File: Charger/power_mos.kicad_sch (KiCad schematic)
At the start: 7 parts, among them Q1 MMBT3906, Q2 AO3400A

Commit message: charger WIP
Most footprints assigned, shunt drawn in schem
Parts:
- renumbered D7 to D9
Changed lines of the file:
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@@
 		(in_pos_files yes)
 		(dnp no)
-		(property "Reference" "D7"
+		(property "Reference" "D9"
 			(at 126.365 86.233 90)
 			(show_name no)
@@
 			(project "Charger"
 				(path "/ba218c5d-b6ee-4635-9cf5-de406e83bbdf/5e21c6b0-7567-43d6-bd0d-213ea70bf189"
-					(reference "D7")
+					(reference "D9")
 					(unit 1)
 				)
 				(path "/ba218c5d-b6ee-4635-9cf5-de406e83bbdf/d20a1503-06d5-45b3-92f8-a558cbee8499"
-					(reference "D8")
+					(reference "D10")
 					(unit 1)
 				)

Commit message: edited VCU and  charger
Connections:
- net VIN: no longer Q1.2 (E)
- new net +5V: Q1.2 (E)
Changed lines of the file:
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@@
-	)
-	(junction
-		(at 130.81 68.58)
-		(diameter 0)
-		(color 0 0 0 0)
 	)
 	(junction
@@
 	(wire
 		(pts
-			(xy 128.27 68.58) (xy 130.81 68.58)
-		)
-		(stroke
-			(width 0)
-			(type default)
-		)
-	)
-	(wire
-		(pts
 			(xy 148.59 72.39) (xy 153.67 72.39)
 		)
@@
 		)
 	)
-	(wire
-		(pts
-			(xy 139.7 68.58) (xy 130.81 68.58)
-		)
-		(stroke
-			(width 0)
-			(type default)
+	(hierarchical_label "VIN"
+		(shape input)
+		(at 139.7 68.58 180)
+		(effects
+			(font
+				(size 1.27 1.27)
+			)
+			(justify right)
 		)
 	)
@@
 			)
 			(justify left)
-		)
-	)
-	(hierarchical_label "VIN"
-		(shape input)
-		(at 128.27 68.58 180)
-		(effects
-			(font
-				(size 1.27 1.27)
-			)
-			(justify right)
 		)
 	)
@@
 					(unit 1)
 				)
+			)
+		)
+	)
+	(symbol
+		(lib_id "power:+5V")
+		(at 130.81 68.58 0)
+		(unit 1)
+		(body_style 1)
+		(exclude_from_sim no)
+		(in_bom yes)
+		(on_board yes)
+		(in_pos_files yes)
+		(dnp no)
+		(fields_autoplaced yes)
+		(property "Reference" "#PWR0103"
+			(at 130.81 72.39 0)
+			(hide yes)
+			(show_name no)
+			(do_not_autoplace no)
+			(effects
+				(font
+					(size 1.27 1.27)
+				)
+			)
+		)
+		(property "Value" "+5V"
+			(at 130.81 63.5 0)
+			(show_name no)
+			(do_not_autoplace no)
+			(effects
+				(font
+					(size 1.27 1.27)
+				)
+			)
+		)
+		(property "Footprint" ""
+			(at 130.81 68.58 0)
+			(hide yes)
+			(show_name no)
+			(do_not_autoplace no)
+			(effects
+				(font
+					(size 1.27 1.27)
+				)
+			)
+		)
+		(property "Datasheet" ""
+			(at 130.81 68.58 0)
+			(hide yes)
+			(show_name no)
+			(do_not_autoplace no)
+			(effects
+				(font
+					(size 1.27 1.27)
+				)
+			)
+		)
+		(property "Description" "Power symbol creates a global label with name \"+5V\""
+			(at 130.81 68.58 0)
+			(hide yes)
+			(show_name no)
+			(do_not_autoplace no)
+			(effects
+				(font
+					(size 1.27 1.27)
+				)
+			)
+		)
+		(pin "1"
+		)
+		(instances
+			(project "Charger"
+				(path "/ba218c5d-b6ee-4635-9cf5-de406e83bbdf/5e21c6b0-7567-43d6-bd0d-213ea70bf189"
+					(reference "#PWR0103")
+					(unit 1)
+				)
+				(path "/ba218c5d-b6ee-4635-9cf5-de406e83bbdf/d20a1503-06d5-45b3-92f8-a558cbee8499"
+					(reference "#PWR0104")
+					(unit 1)
+				)

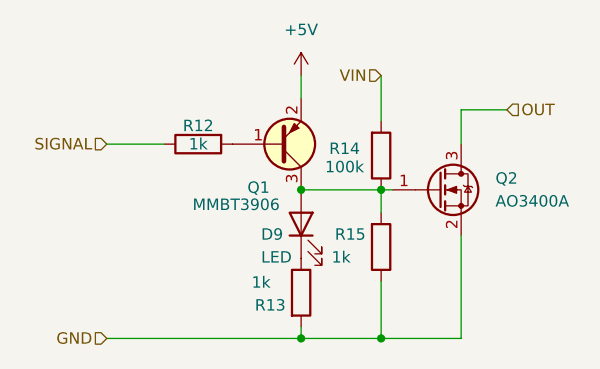
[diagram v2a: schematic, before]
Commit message: Charger 0.1.0 PCB ready for review
Silkscreen adjustments have not been finished yet
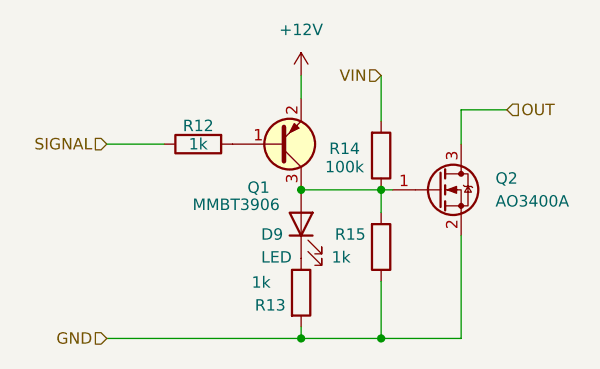
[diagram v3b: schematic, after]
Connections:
- net +5V renamed +12V
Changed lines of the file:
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@@
 	(generator_version "10.0")
 	(paper "A4")
+	(title_block
+		(date "2026-08-20")
+		(rev "0.1.1")
+	)
 	(junction
 		(at 130.81 81.28)
@@
 				(path "/ba218c5d-b6ee-4635-9cf5-de406e83bbdf/d20a1503-06d5-45b3-92f8-a558cbee8499"
 					(reference "R17")
-					(unit 1)
-				)
-			)
-		)
-	)
-	(symbol
-		(lib_id "power:+5V")
-		(at 130.81 68.58 0)
-		(unit 1)
-		(body_style 1)
-		(exclude_from_sim no)
-		(in_bom yes)
-		(on_board yes)
-		(in_pos_files yes)
-		(dnp no)
-		(fields_autoplaced yes)
-		(property "Reference" "#PWR0103"
-			(at 130.81 72.39 0)
-			(hide yes)
-			(show_name no)
-			(do_not_autoplace no)
-			(effects
-				(font
-					(size 1.27 1.27)
-				)
-			)
-		)
-		(property "Value" "+5V"
-			(at 130.81 63.5 0)
-			(show_name no)
-			(do_not_autoplace no)
-			(effects
-				(font
-					(size 1.27 1.27)
-				)
-			)
-		)
-		(property "Footprint" ""
-			(at 130.81 68.58 0)
-			(hide yes)
-			(show_name no)
-			(do_not_autoplace no)
-			(effects
-				(font
-					(size 1.27 1.27)
-				)
-			)
-		)
-		(property "Datasheet" ""
-			(at 130.81 68.58 0)
-			(hide yes)
-			(show_name no)
-			(do_not_autoplace no)
-			(effects
-				(font
-					(size 1.27 1.27)
-				)
-			)
-		)
-		(property "Description" "Power symbol creates a global label with name \"+5V\""
-			(at 130.81 68.58 0)
-			(hide yes)
-			(show_name no)
-			(do_not_autoplace no)
-			(effects
-				(font
-					(size 1.27 1.27)
-				)
-			)
-		)
-		(pin "1"
-		)
-		(instances
-			(project "Charger"
-				(path "/ba218c5d-b6ee-4635-9cf5-de406e83bbdf/5e21c6b0-7567-43d6-bd0d-213ea70bf189"
-					(reference "#PWR0103")
-					(unit 1)
-				)
-				(path "/ba218c5d-b6ee-4635-9cf5-de406e83bbdf/d20a1503-06d5-45b3-92f8-a558cbee8499"
-					(reference "#PWR0104")
 					(unit 1)
 				)
@@
 					(unit 1)
 				)
+			)
+		)
+	)
+	(symbol
+		(lib_id "power:+12V")
+		(at 130.81 68.58 0)
+		(unit 1)
+		(body_style 1)
+		(exclude_from_sim no)
+		(in_bom yes)
+		(on_board yes)
+		(in_pos_files yes)
+		(dnp no)
+		(fields_autoplaced yes)
+		(property "Reference" "#PWR010"
+			(at 130.81 72.39 0)
+			(hide yes)
+			(show_name no)
+			(do_not_autoplace no)
+			(effects
+				(font
+					(size 1.27 1.27)
+				)
+			)
+		)
+		(property "Value" "+12V"
+			(at 130.81 63.5 0)
+			(show_name no)
+			(do_not_autoplace no)
+			(effects
+				(font
+					(size 1.27 1.27)
+				)
+			)
+		)
+		(property "Footprint" ""
+			(at 130.81 68.58 0)
+			(hide yes)
+			(show_name no)
+			(do_not_autoplace no)
+			(effects
+				(font
+					(size 1.27 1.27)
+				)
+			)
+		)
+		(property "Datasheet" ""
+			(at 130.81 68.58 0)
+			(hide yes)
+			(show_name no)
+			(do_not_autoplace no)
+			(effects
+				(font
+					(size 1.27 1.27)
+				)
+			)
+		)
+		(property "Description" "Power symbol creates a global label with name \"+12V\""
+			(at 130.81 68.58 0)
+			(hide yes)
+			(show_name no)
+			(do_not_autoplace no)
+			(effects
+				(font
+					(size 1.27 1.27)
+				)
+			)
+		)
+		(pin "1"
+		)
+		(instances
+			(project "Charger"
+				(path "/ba218c5d-b6ee-4635-9cf5-de406e83bbdf/5e21c6b0-7567-43d6-bd0d-213ea70bf189"
+					(reference "#PWR010")
+					(unit 1)
+				)
+				(path "/ba218c5d-b6ee-4635-9cf5-de406e83bbdf/d20a1503-06d5-45b3-92f8-a558cbee8499"
+					(reference "#PWR023")
+					(unit 1)
+				)

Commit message: push stuffs
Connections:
- net +12V renamed +5V
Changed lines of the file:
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@@
+	)
+	(symbol
+		(lib_id "power:+5V")
+		(at 130.81 68.58 0)
+		(unit 1)
+		(body_style 1)
+		(exclude_from_sim no)
+		(in_bom yes)
+		(on_board yes)
+		(in_pos_files yes)
+		(dnp no)
+		(fields_autoplaced yes)
+		(property "Reference" "#PWR010"
+			(at 130.81 72.39 0)
+			(hide yes)
+			(show_name no)
+			(do_not_autoplace no)
+			(effects
+				(font
+					(size 1.27 1.27)
+				)
+			)
+		)
+		(property "Value" "+5V"
+			(at 130.81 63.5 0)
+			(show_name no)
+			(do_not_autoplace no)
+			(effects
+				(font
+					(size 1.27 1.27)
+				)
+			)
+		)
+		(property "Footprint" ""
+			(at 130.81 68.58 0)
+			(hide yes)
+			(show_name no)
+			(do_not_autoplace no)
+			(effects
+				(font
+					(size 1.27 1.27)
+				)
+			)
+		)
+		(property "Datasheet" ""
+			(at 130.81 68.58 0)
+			(hide yes)
+			(show_name no)
+			(do_not_autoplace no)
+			(effects
+				(font
+					(size 1.27 1.27)
+				)
+			)
+		)
+		(property "Description" "Power symbol creates a global label with name \"+5V\""
+			(at 130.81 68.58 0)
+			(hide yes)
+			(show_name no)
+			(do_not_autoplace no)
+			(effects
+				(font
+					(size 1.27 1.27)
+				)
+			)
+		)
+		(pin "1"
+		)
+		(instances
+			(project "Charger"
+				(path "/ba218c5d-b6ee-4635-9cf5-de406e83bbdf/5e21c6b0-7567-43d6-bd0d-213ea70bf189"
+					(reference "#PWR010")
+					(unit 1)
+				)
+				(path "/ba218c5d-b6ee-4635-9cf5-de406e83bbdf/d20a1503-06d5-45b3-92f8-a558cbee8499"
+					(reference "#PWR023")
+					(unit 1)
+				)
+			)
+		)
 	)
 	(symbol
@@
 					(unit 1)
 				)
-			)
-		)
-	)
-	(symbol
-		(lib_id "power:+12V")
-		(at 130.81 68.58 0)
-		(unit 1)
-		(body_style 1)
-		(exclude_from_sim no)
-		(in_bom yes)
-		(on_board yes)
-		(in_pos_files yes)
-		(dnp no)
-		(fields_autoplaced yes)
-		(property "Reference" "#PWR010"
-			(at 130.81 72.39 0)
-			(hide yes)
-			(show_name no)
-			(do_not_autoplace no)
-			(effects
-				(font
-					(size 1.27 1.27)
-				)
-			)
-		)
-		(property "Value" "+12V"
-			(at 130.81 63.5 0)
-			(show_name no)
-			(do_not_autoplace no)
-			(effects
-				(font
-					(size 1.27 1.27)
-				)
-			)
-		)
-		(property "Footprint" ""
-			(at 130.81 68.58 0)
-			(hide yes)
-			(show_name no)
-			(do_not_autoplace no)
-			(effects
-				(font
-					(size 1.27 1.27)
-				)
-			)
-		)
-		(property "Datasheet" ""
-			(at 130.81 68.58 0)
-			(hide yes)
-			(show_name no)
-			(do_not_autoplace no)
-			(effects
-				(font
-					(size 1.27 1.27)
-				)
-			)
-		)
-		(property "Description" "Power symbol creates a global label with name \"+12V\""
-			(at 130.81 68.58 0)
-			(hide yes)
-			(show_name no)
-			(do_not_autoplace no)
-			(effects
-				(font
-					(size 1.27 1.27)
-				)
-			)
-		)
-		(pin "1"
-		)
-		(instances
-			(project "Charger"
-				(path "/ba218c5d-b6ee-4635-9cf5-de406e83bbdf/5e21c6b0-7567-43d6-bd0d-213ea70bf189"
-					(reference "#PWR010")
-					(unit 1)
-				)
-				(path "/ba218c5d-b6ee-4635-9cf5-de406e83bbdf/d20a1503-06d5-45b3-92f8-a558cbee8499"
-					(reference "#PWR023")
-					(unit 1)
-				)
